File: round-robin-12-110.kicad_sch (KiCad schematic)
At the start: 242 parts

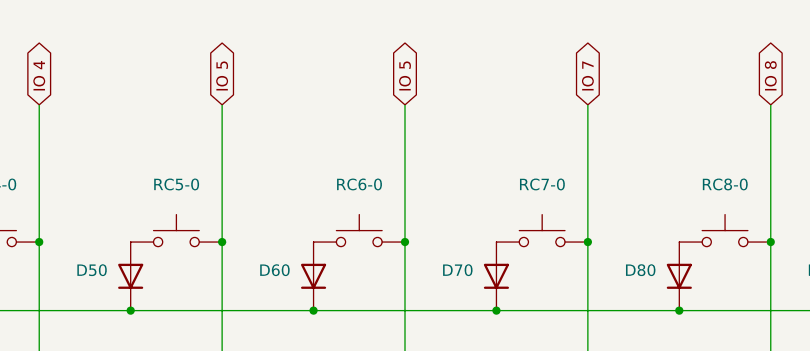
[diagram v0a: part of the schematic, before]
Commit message: fix: rename duplicated IO5 label
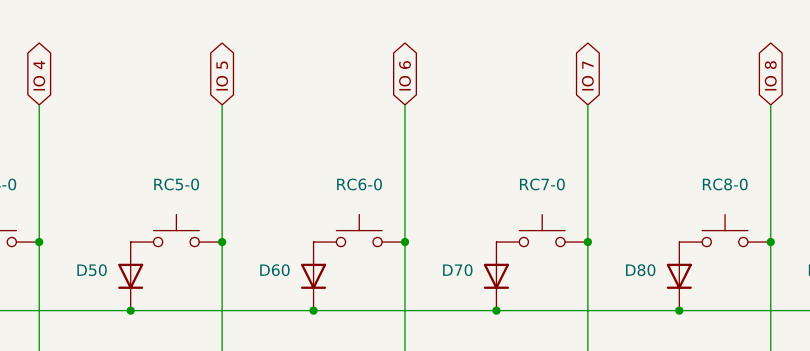
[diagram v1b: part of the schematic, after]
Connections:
- net IO 5: no longer DS6.1 (K), RC6-0.1, RC6-1.1, RC6-2.1, RC6-3.1, RC6-4.1, RC6-5.1, RC6-6.1, RC6-7.1, RC6-8.1, RC6-9.1
- new net IO 6: DS6.1 (K), RC6-0.1, RC6-1.1, RC6-2.1, RC6-3.1, RC6-4.1, RC6-5.1, RC6-6.1, RC6-7.1, RC6-8.1, RC6-9.1
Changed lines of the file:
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@@
 		)
 	)
-	(global_label "IO 5"
+	(global_label "IO 6"
 		(shape bidirectional)
 		(at 165.1 25.4 90)
@@
 		)
 		(property "Intersheetrefs" "${INTERSHEET_REFS}"
-			(at 165.1 17.2705 90)
+			(at 165.1 17.1911 90)
 			(effects
 				(font
 					(size 1.27 1.27)
 				)
-				(justify right)
+				(justify left)
 				(hide yes)
 			)
